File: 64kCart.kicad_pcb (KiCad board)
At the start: 2 copper layers, 58.2 x 49.9 mm, 11 parts, among them SW1 Reset, U1 27C512, U2 74LS173, U3 74LS04, U4 C64-Exp-Port

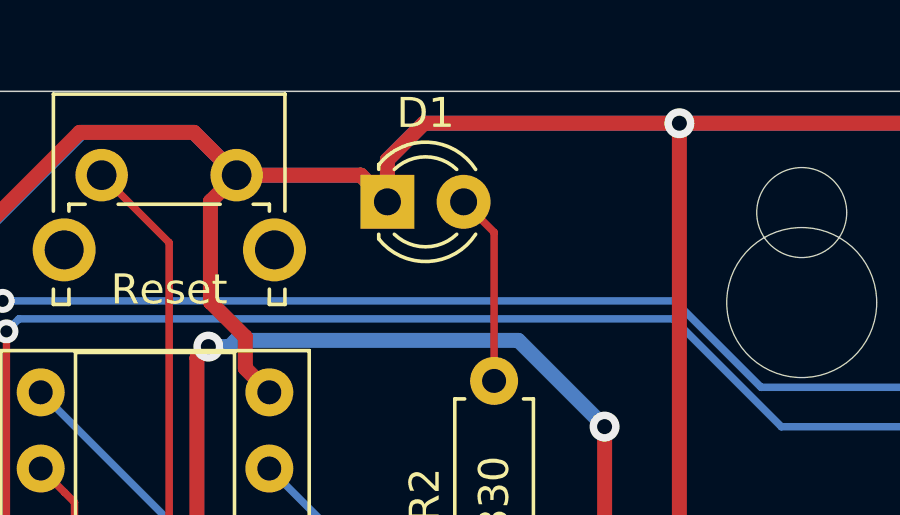
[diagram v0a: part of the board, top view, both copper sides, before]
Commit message: Mark LED orientation.
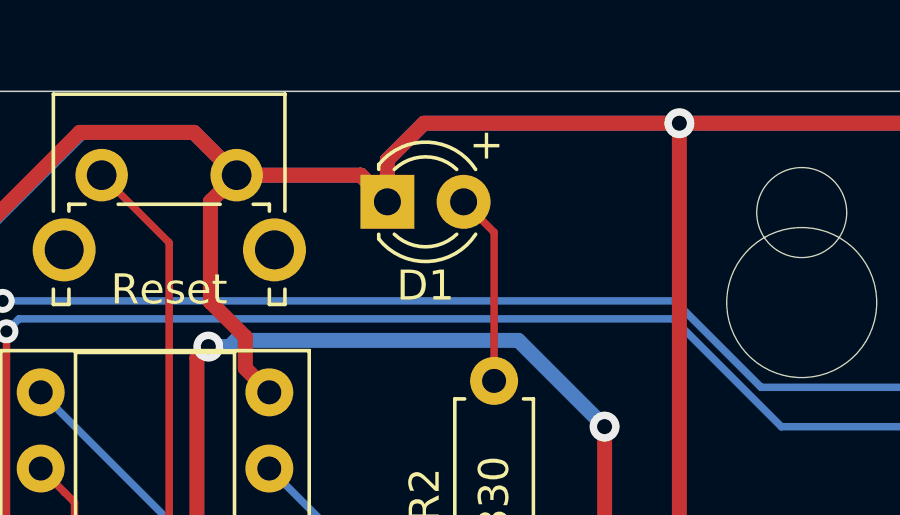
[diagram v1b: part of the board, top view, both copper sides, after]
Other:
- board text added: "+"
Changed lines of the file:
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@@
   (general
     (thickness 1.6)
-    (drawings 13)
+    (drawings 14)
     (tracks 346)
     (zones 0)
@@
     (descr "LED, diameter 3.0mm, 2 pins")
     (tags "LED diameter 3.0mm 2 pins")
-    (fp_text reference D1 (at 1.27 -2.96) (layer F.SilkS)
+    (fp_text reference D1 (at 1.27 2.794) (layer F.SilkS)
       (effects (font (size 1 1) (thickness 0.15)))
     )
@@
     (pad "" np_thru_hole circle (at 0 -3) (size 3 3) (drill 3) (layers *.Cu *.Mask))
   )
+  (gr_text + (at 126.365 90.678) (layer F.SilkS)
+    (effects (font (size 1 1) (thickness 0.15)))
+  )
   (gr_text "64kCart Remix 2019 Rev.1 - https://www.hackup.net\nBased on the original \"64k Karte\" design by Hucky." (at 160.5915 127.762) (layer B.SilkS)

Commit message: Minor updates for revision 2.
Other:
- board text added: "2019 Rev.2"
- board text removed: "2019 Rev.1"
